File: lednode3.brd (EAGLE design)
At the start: 49.8 x 50 mm, 23 parts, among them SW1 EC12E_SW, U1 LCD-16X2NOHOLES

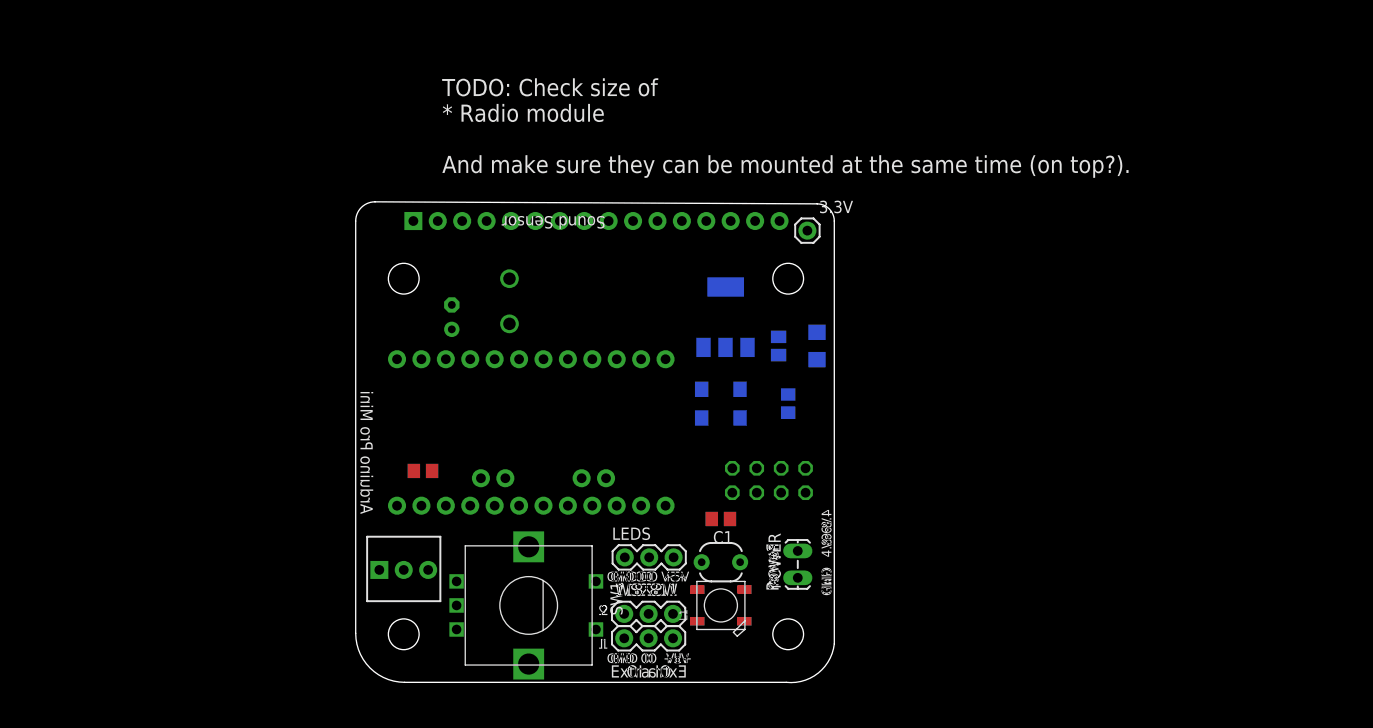
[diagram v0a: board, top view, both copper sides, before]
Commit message: Started working on smaller ledboard. Some updates to controll board.
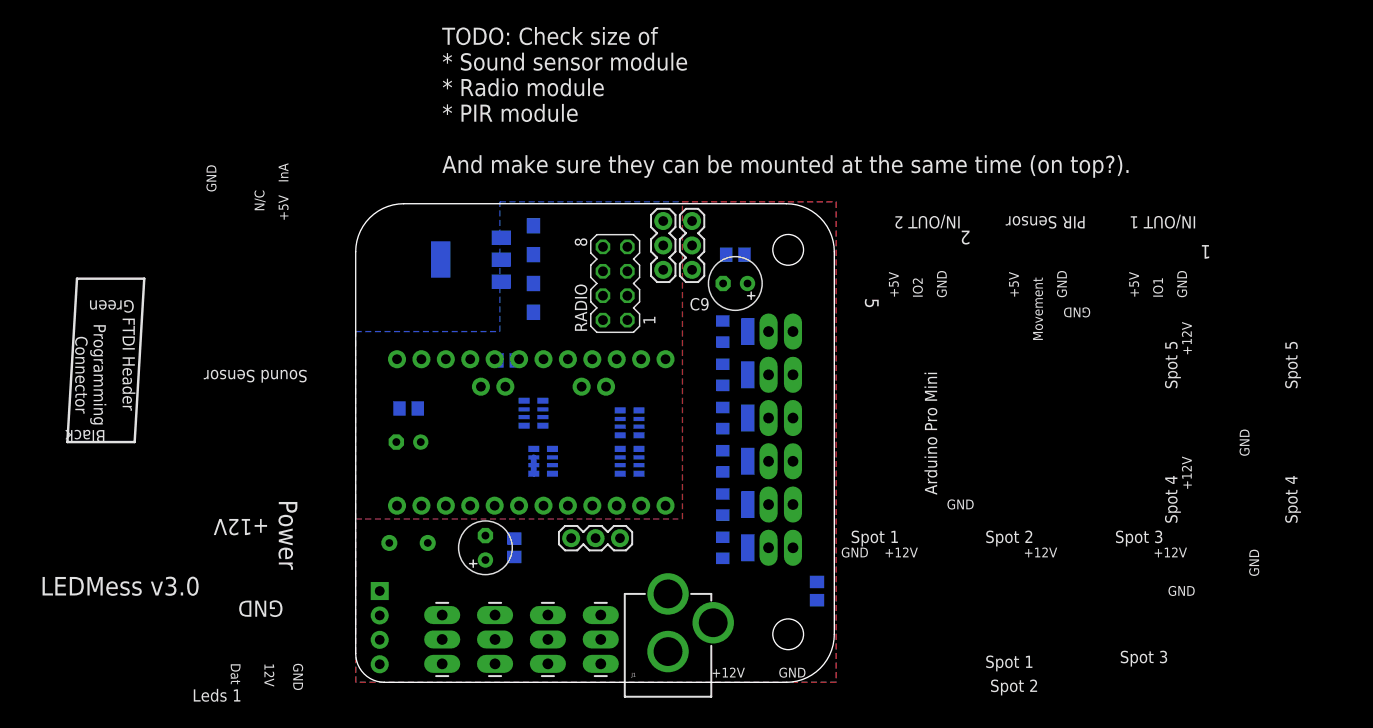
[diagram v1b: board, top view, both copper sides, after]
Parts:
- removed 3.3V: M01PTH, SparkFun-Connectors:1X01
- removed C10, C8: 100 nF, rcl:C0805
- removed C15: 100 uF, rcl:E2,5-6
- removed L1: WS2812B, adafruit:WS2812B
- removed LEDS: (no value), SparkFun-Connectors:1X03
- removed POWER: (no value), SparkFun:1X02_LOCK_LONGPADS
- removed POWERLED: (no value), led:1206
- removed R1: 10k, SparkFun:3362U-2
- removed R3: 100R, rcl:M0805
- removed S1: CM4400, sensor-comus-group:CM4400
- removed SW1: EC12E_SW, switch-alps:ALPS_EC12E_SW
- removed U1: LCD-16X2NOHOLES, SparkFun:LCD-16X2_NOHOLES
- added C2, C3, C5, C6: 100 nF, rcl:C0805
- added C4, C9: 100 uF, rcl:E2,5-6
- added C7: 22uF, Tantalum, rcl:SMC_A
- added J1: POWER_JACKPTH, SparkFun-Connectors:POWER_JACK_PTH
- added LEDS1, LEDS2, LEDS3, LEDS4: (no value), SparkFun-Connectors:1X03_LONGPADS
- added PIR: (no value), SparkFun-Connectors:1X03
- added Q1, Q2, Q3, Q4, Q5, Q6: AO3402, adafruit:SOT23-W
- added RN1, RN3: 220R, dp_devices:RN8P-4R-CRA06S
- added RN2, RN4: 10k, dp_devices:RN8P-4R-CRA06S
- added SOUND_SENSOR: (no value), SparkFun-Connectors:1X04_NO_SILK
- added SPOT1, SPOT2, SPOT3, SPOT4, SPOT5, SPOT6: M02PTH3, SparkFun-Connectors:1X02_LONGPADS
- C1: value 100 nF -> 100 uF; device rcl:C0805 -> rcl:E2,5-6
- C12: value 22uF, Tant -> 22uF, Tantalum
- C13: value (22uF, Tant) -> 100 nF; device rcl:SMC_A -> rcl:C0805
- moved LOGO3 45.5 mm to (59.5, 1.50)
- moved IO2 43.6 mm to (32.0, 48.0), turned to 270 degrees
- moved IO1 41.5 mm to (35.0, 48.0), turned to 270 degrees
- moved PHOTOCELL 32.6 mm to (5.50, 14.5), flipped to the bottom, turned to 180 degrees
- moved C12 27.4 mm to (18.5, 46.0), turned to 90 degrees
- moved 3.3V_REGULATOR 27.2 mm to (12.0, 44.0), turned to 270 degrees
- moved RADIO 26.0 mm to (27.0, 41.5), flipped to the top, turned to 90 degrees
- moved C1 24.7 mm to (13.5, 14.0), turned to 90 degrees
- moved C13 22.9 mm to (48.0, 9.50), turned to 90 degrees
- flipped U$1 to the top, turned to 90 degrees
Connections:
- removed net LCD_BACKLIGHT: U$1.13, U1.16
- removed net LCD_CONTRAST: R1.2, U1.3
- removed net LCD_DATA4: U$1.7, U1.11
- removed net LCD_DATA5: U$1.8, U1.12
- removed net LCD_DATA6: U$1.9, U1.13
- removed net LCD_DATA7: U$1.10, U1.14
- removed net LCD_ENABLE: U$1.6, U1.6
- removed net LCD_RS: U$1.5, U1.4
- removed net LEDSTRIP_OUT: L1.2-DOUT, LEDS.2
- removed net ROTARY_A: SW1.A, U$1.11
- removed net ROTARY_B: SW1.B, U$1.12
- removed net ROTARY_PUSH: SW1.D, U$1.19
- removed net SHAKE_SENSOR: S1.2, U$1.A6
- removed net STATUS_LED: L1.4-DIN, U$1.20
- removed net V+: POWER.2, R1.1, U1.2
- new net +12V: C1.+, C3.1, C5.1, C6.1, C9.+, J1.PWR, LEDS1.1, LEDS2.1, LEDS3.1, LEDS4.1, SPOT1.1, SPOT2.1, SPOT3.1, SPOT4.1, SPOT5.1, SPOT6.1, U$1.24
- new net LEDSTRIP1: LEDS1.2, U$1.5
- new net LEDSTRIP2: LEDS2.2, U$1.7
- new net LEDSTRIP3: LEDS3.2, U$1.10
- new net LEDSTRIP4: LEDS4.2, U$1.11
- new net N$10: Q5.1, RN3.6
- new net N$11: Q6.3, SPOT6.2
- new net N$12: RN4.3, RN4.4
- new net N$14: Q6.1, RN3.8
- new net N$2: Q1.3, SPOT1.2
- new net N$3: Q2.3, SPOT2.2
- new net N$4: Q4.3, SPOT4.2
- new net N$5: Q3.3, SPOT3.2
- new net N$6: Q1.1, RN1.8
- new net N$7: Q2.1, RN1.7
- new net N$8: Q4.1, RN3.7
- new net N$9: Q3.1, RN1.6
- new net PROXIMITY: PIR.2, U$1.A6
- new net SOUND_ANALOG: SOUND_SENSOR.1, U$1.19
- new net SOUND_TRESHOLD: SOUND_SENSOR.4
- new net SPOTLIGHT1: RN1.1, RN2.8, U$1.6
- new net SPOTLIGHT2: RN1.2, RN2.7, U$1.8
- new net SPOTLIGHT3: RN1.3, RN2.6, U$1.9
- new net SPOTLIGHT4: RN2.5, RN3.2, U$1.12
- new net SPOTLIGHT5: RN3.3, RN4.8, U$1.13
- new net SPOTLIGHT6: RN3.1, RN4.7, U$1.20
- net +3V3: now also C13.1, RN3.5; no longer 3.3V.1, C10.1, POWERLED.A
- net +5V: now also C2.1, C4.+, C7.+, PHOTOCELL.2, PIR.3, SOUND_SENSOR.3; no longer C1.1, C13.+, C15.+, C8.1, L1.1-VDD, LEDS.3, U1.15
- net GND: now also C1.-, C13.2, C2.2, C3.2, C4.-, C5.2, C6.2, C7.-, C9.-, J1.GND, J1.GNDBREAK, LEDS1.3, LEDS2.3, LEDS3.3, LEDS4.3, PIR.1, Q1.2, Q2.2, Q3.2, Q4.2, Q5.2, Q6.2, RN2.1, RN2.2, RN2.3, RN2.4, RN3.4, RN4.1, RN4.2, RN4.6, SOUND_SENSOR.2; no longer C1.2, C10.2, C13.-, C15.-, C8.2, L1.3-GND, LEDS.1, PHOTOCELL.1, POWER.1, R1.3, R3.1, S1.1, SW1.C, SW1.E, SW1.GND1, SW1.GND2, U1.1, U1.5
- net LIGHTLEVEL: now also PHOTOCELL.1, RN4.5; no longer PHOTOCELL.2
- net N$1: now also Q5.3, SPOT5.2; no longer POWERLED.C, R3.2
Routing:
- net GND: track 0.00 -> 1.70 mm
- added copper zone on layer 1, net +12V
- added copper zone on layer 16, net GND
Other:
- board size 49.8 x 50 mm -> 49.8 x 49.8 mm
- board text added: "+12V"
- board text added: "12V"
- board text added: "5"
- board text added: "Black"
- board text added: "Dat"
- board text added: "FTDI Header"
- board text added: "Green"
- board text added: "IN/OUT 1"
- board text added: "IN/OUT 2"
- board text added: "IO1"
- board text added: "IO2"
- board text added: "InA"
- board text added: "LEDMess Node v2.0"
- board text added: "LEDMess v3.0"
- board text added: "Leds 1"
- board text added: "Movement"
- board text added: "N/C"
- board text added: "PIR Sensor"
- board text added: "Programming Connector"
- board text added: "RST"
- board text added: "RXI"
- board text added: "Spot 1"
- board text added: "Spot 2"
- board text added: "Spot 3"
- board text added: "Spot 4"
- board text added: "Spot 5"
- board text added: "TODO: Check size of * Sound sensor module * Radio module * PIR module And make sure they can be mounted at the same time (on top?)."
- board text added: "TXO"
- board text removed: "+"
- board text removed: "+3.3V"
- board text removed: "10k"
- board text removed: "4.8-6V"
- board text removed: "DO"
- board text removed: "Extra IO"
- board text removed: "IO"
- board text removed: "LED"
- board text removed: "LedController v0.3"
- board text removed: "TODO: Check size of * Radio module And make sure they can be mounted at the same time (on top?)."
- board text removed: "WS2811"
- board text removed: "WS2812B"

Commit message: Finished lednode v 3.0.
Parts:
- removed 3.3V_REGULATOR: AMS1117-3.3, burr-brown:SOT223
- added 3.3V_REG: AMS1117-3.3, burr-brown:SOT223
- added C10: 100 nF, rcl:C0805
- added C8: 100 uF, rcl:E2,5-6
- C12, C7: value 22uF, Tantalum -> 22uF Tant
- IO1, IO2: device SparkFun-Connectors:1X03 -> SparkFun-Connectors:1X05
- moved LOGO3 69.6 mm to (0.75, 38.8), turned to 90 degrees
- moved C13 44.4 mm to (22.8, 46.0)
- moved C5 9.82 mm to (6.20, 31.0)
- moved IO1 4.18 mm to (31.0, 46.8), turned to 0 degrees
- moved IO2 3.86 mm to (31.0, 44.3), turned to 0 degrees
- moved RN2 3.25 mm to (16.2, 23.0)
- moved C6 3.16 mm to (40.5, 41.5), turned to 180 degrees
- moved C9 2.57 mm to (37.2, 40.2), turned to 270 degrees
- moved C4 2.55 mm to (6.00, 22.5), turned to 180 degrees
- moved RN4 2.30 mm to (16.2, 27.5)
- moved C12 2.00 mm to (20.5, 46.0)
- moved C7 2.00 mm to (20.5, 40.0)
- moved RN3 1.58 mm to (30.0, 27.5)
- moved RN1 1.50 mm to (30.0, 23.0)
- moved C1 1.00 mm to (13.5, 13.0)
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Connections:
- new net N$13: Q6.1, RN3.7
- net +12V: now also C10.1, C8.+, IO1.5, IO2.5
- net +3V3: now also 3.3V_REG.2, IO1.3, IO2.3; no longer 3.3V_REGULATOR.2
- net +5V: now also 3.3V_REG.3, IO1.4, IO2.4; no longer 3.3V_REGULATOR.3, IO1.3, IO2.3
- net GND: now also 3.3V_REG.1, C10.2, C8.-, RN3.6; no longer 3.3V_REGULATOR.1, RN3.4
- net N$10: now also RN3.8; no longer RN3.6
- net N$14: now also RN3.3, RN3.4; no longer Q6.1, RN3.8
- net N$8: now also RN1.5; no longer RN3.7
- net SPOTLIGHT4: now also RN1.4; no longer RN3.2
- net SPOTLIGHT5: now also RN3.1; no longer RN3.3
- net SPOTLIGHT6: now also RN3.2; no longer RN3.1
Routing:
- net GND: track 1.70 -> 134.6 mm
- net +5V: track 0.00 -> 109.7 mm, vias 0 -> 4
- net +12V: track 0.00 -> 98.1 mm, vias 0 -> 1
- net +3V3: track 0.00 -> 47.9 mm, vias 0 -> 2
- net EXTRA_IO2: track 0.00 -> 39.0 mm, vias 0 -> 2
- net SOUND_ANALOG: track 0.00 -> 37.4 mm, vias 0 -> 2
- net EXTRA_IO1: track 0.00 -> 37.3 mm, vias 0 -> 2
- net LIGHTLEVEL: track 0.00 -> 37.0 mm, vias 0 -> 2
- net PROXIMITY: track 0.00 -> 30.7 mm
- net SPOTLIGHT6: track 0.00 -> 24.1 mm, vias 0 -> 1
- net LEDSTRIP1: track 0.00 -> 23.8 mm, vias 0 -> 2
- net SPOTLIGHT4: track 0.00 -> 23.6 mm, vias 0 -> 1
- net SPOTLIGHT5: track 0.00 -> 22.3 mm, vias 0 -> 2
- net LEDSTRIP3: track 0.00 -> 21.6 mm, vias 0 -> 2
- net SPOTLIGHT3: track 0.00 -> 17.8 mm, vias 0 -> 1
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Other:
- outline, holes or cut-outs redrawn
- board text added: "+"
- board text added: "-"
- board text added: "3"
- board text added: "3.3V"
- board text added: "4"
- board text added: "4 WS2811 LED Strips"
- board text added: "5V"
- board text added: "6"
- board text added: "6 Spotlights or 2 Single Color RGB Strips"
- board text added: "Extra IO"
- board text added: "IO"
- board text added: "LDR"
- board text added: "LED Node v3.0"
- board text added: "NRF24L01"
- board text added: "On/Off"
- board text added: "Radio"
- board text added: "Sound"
- board text added: "github.com/zzorn/ledmesh"
- board text removed: "Black"
- board text removed: "FTDI Header"
- board text removed: "Green"
- board text removed: "IN/OUT 1"
- board text removed: "IN/OUT 2"
- board text removed: "IO1"
- board text removed: "IO2"
- board text removed: "InA"
- board text removed: "LEDMess Node v2.0"
- board text removed: "LEDMess v3.0"
- board text removed: "Leds 1"
- board text removed: "Movement"
- board text removed: "Programming Connector"
- board text removed: "RST"
- board text removed: "RXI"
- board text removed: "Spot 1"
- board text removed: "Spot 2"
- board text removed: "Spot 3"
- board text removed: "Spot 4"
- board text removed: "Spot 5"
- board text removed: "TODO: Check size of * Sound sensor module * Radio module * PIR module And make sure they can be mounted at the same time (on top?)."
- board text removed: "TXO"
- board text removed: "github.com/zzorn/ledmess"
